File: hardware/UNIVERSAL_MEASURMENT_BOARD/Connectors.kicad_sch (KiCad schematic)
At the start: 43 parts, among them J1 2606-1110_010-000, J2 2606-1110_010-000, J28 FTSH-107-01-L-D-K, J3 2606-1110_010-000, J4 2606-1110_010-000, J5 2604-1104, U17 ESDS304DBVR, U18 ESDS304DBVR

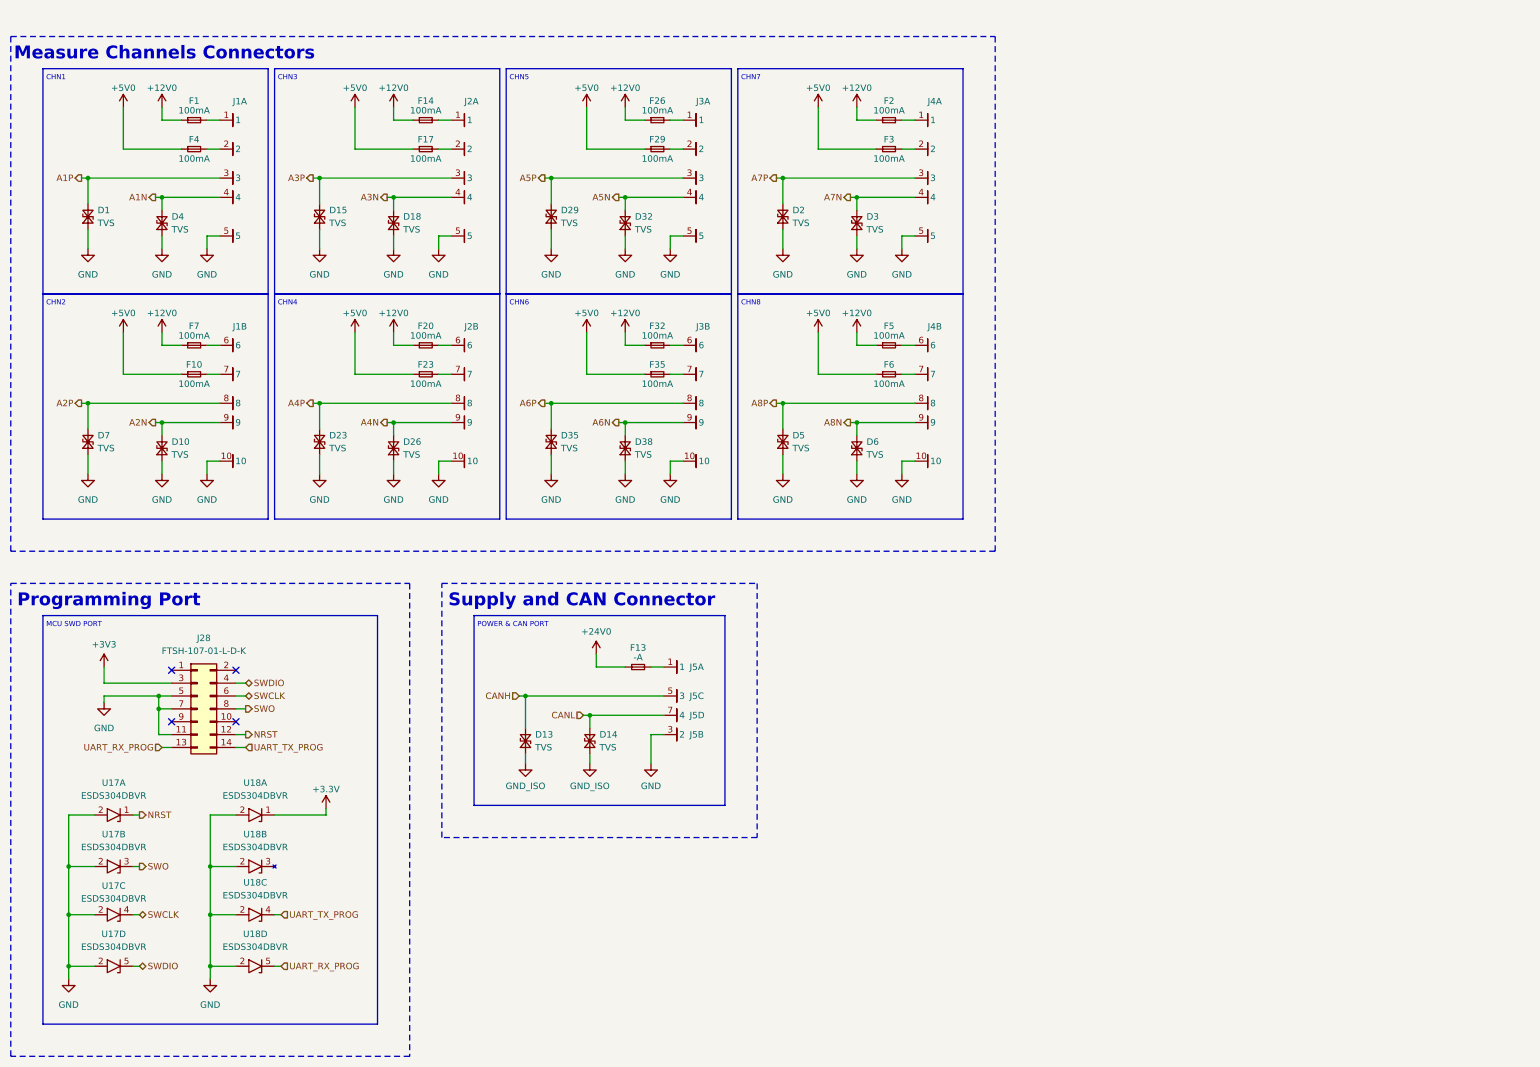
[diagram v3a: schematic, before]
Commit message: added footprints
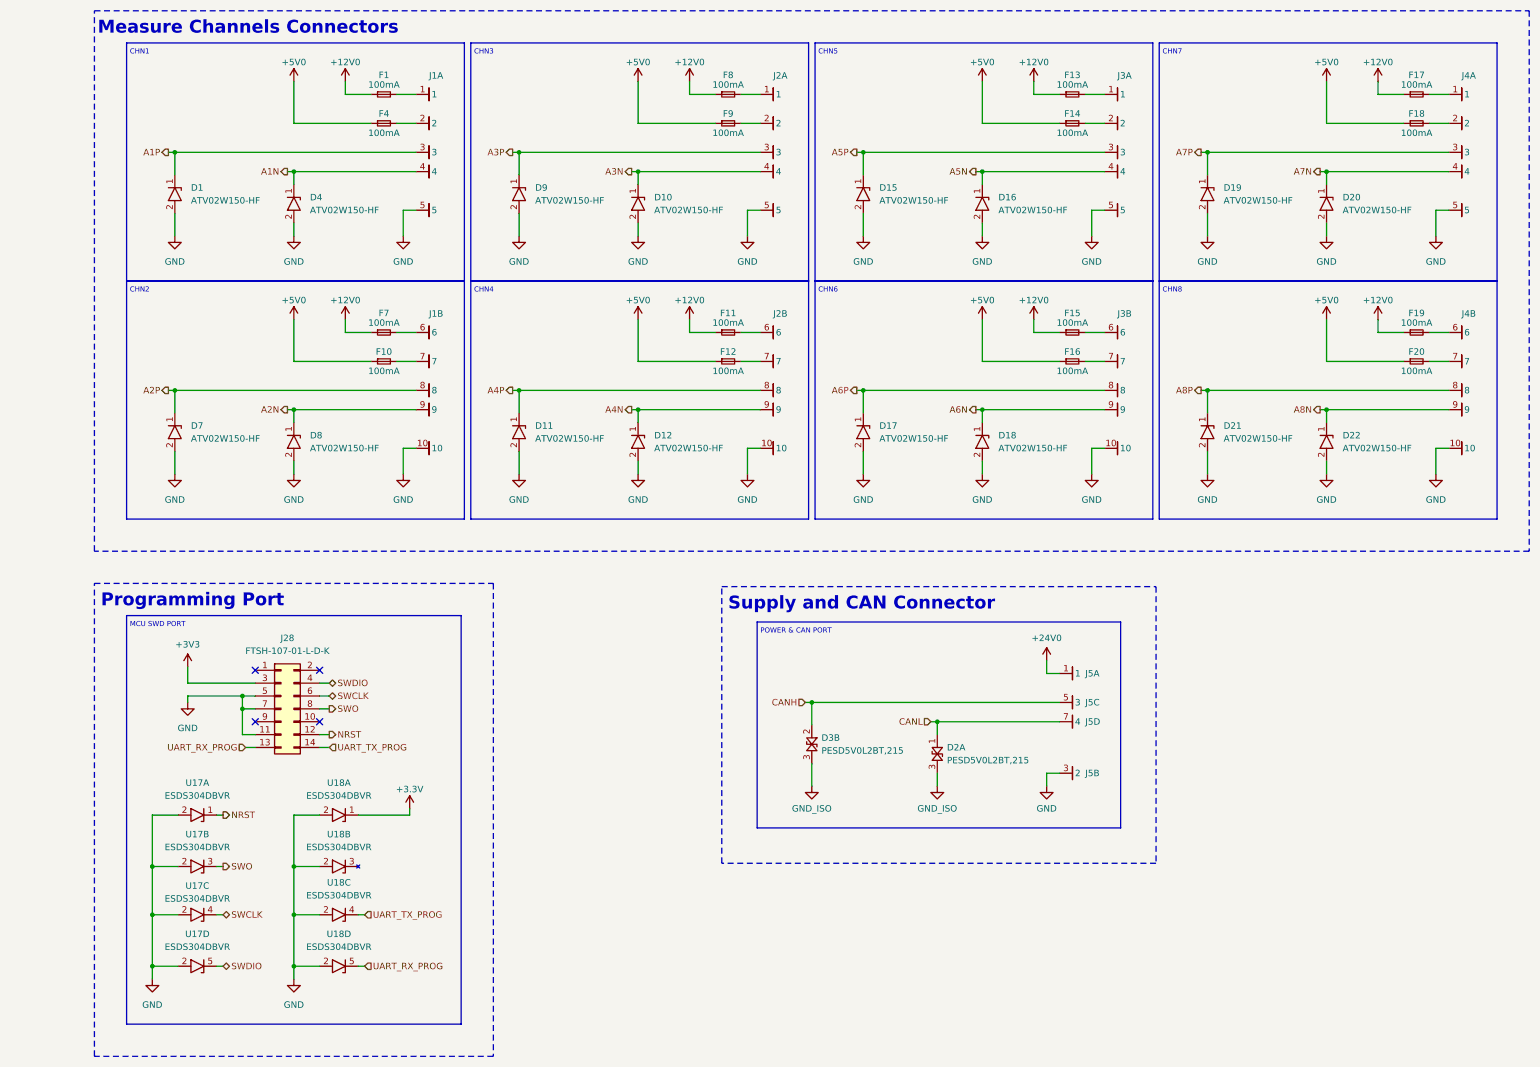
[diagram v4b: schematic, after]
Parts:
- removed D1, D10, D13, D14, D15, D18, D2, D23, D26, D29, D3, D32, D35, D38, D4, D5, D6, D7: TVS, symbol Device:D_TVS_Small
- removed F2, F23, F26, F29, F3, F32, F35, F5, F6: 100mA, symbol Device:Fuse_Small
- added D1, D10, D11, D12, D15, D16, D17, D18, D19, D20, D21, D22, D4, D7, D8, D9: ATV02W150-HF, SODFL3718X130N, symbol ATV02W150-HF:ATV02W150-HF
- added D2, D3: PESD5V0L2BT,215, SOT95P230X110-3N, symbol PESD5V0L2BT,215:PESD5V0L2BT,215
- added F11, F12, F15, F16, F18, F19, F8, F9: 100mA, Resistor_SMD:R_0603_1608Metric, symbol Device:Fuse_Small
- F1, F10, F14, F17, F20, F4, F7: footprint (none) -> Resistor_SMD:R_0603_1608Metric
- F13: value -A -> 100mA; footprint (none) -> Resistor_SMD:R_0603_1608Metric
- J28: footprint Samacsys:FTSH-107-XX-YYY-D-K -> FTSH-107-01-L-D-K:FTSH-107-XX-YYY-D-K
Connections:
- net +12V0: now also F13.1, F17.1, F11.1, F15.1, F19.1, F8.1; no longer F14.1, F20.1
- net +24V0: now also J5.1, J5.2 (1.2); no longer F13.1
- net +5V0: now also F14.1, F20.1, F12.1, F16.1, F18.1, F9.1; no longer F17.1
- net A1N: now also D4.1
- net A1P: now also D1.1
- net A2N: now also D8.1
- net A2P: now also D7.1
- net A3N: now also D10.1
- net A3P: now also D9.1
- net A4N: now also D12.1
- net A4P: now also D11.1
- net A5N: now also D16.1
- net A5P: now also D15.1
- net A6N: now also D18.1
- net A6P: now also D17.1
- net A7N: now also D20.1
- net A7P: now also D19.1
- net A8N: now also D22.1
- net A8P: now also D21.1
- net CANH: now also D3.2
- net CANL: now also D2.1
- net GND: now also D1.2, D10.2, D11.2, D12.2, D15.2, D16.2, D17.2, D18.2, D19.2, D20.2, D21.2, D22.2, D4.2, D7.2, D8.2, D9.2
- net GND_ISO: now also D2.3, D3.3
- net at J4.7: now also F20.2
- net at J3.7: now also F16.2
- net at J3.6: now also F15.2
- net at J4.6: now also F19.2
- net at J3.1: now also F13.2
- net at J2.7: now also F12.2
- net at J4.2: now also F18.2
- net at J2.6: now also F11.2; no longer F20.2
- net at J2.1: now also F8.2; no longer F14.2
- net at F17.2: now also J4.1; no longer J2.2
- net at J3.2: now also F14.2
- new net: F9.2, J2.2
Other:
- company: PUT Motorsport Formula Student team -> PUT Motorsport Formula Student Team
- moved on the sheet: F10, F7, J1A, J1B, J28, J2A, J2B, J3A, J3B, J4A, J4B, J5A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

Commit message: first outcom of pcb design
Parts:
- removed J5: 2604-1104, 2601-1104:26011104, symbol 2601-1104:2604-1104
- removed unit 2 of U17
- removed unit 4 of U18
- removed unit 3 of U18
- removed unit 1 of U18
- added J4, J5, J6, J7: Conn_01x01_Socket, REST:SolderWire-0.1sqmm_1x01_D0.4mm_OD1mm_Relief2x, symbol Connector:Conn_01x01_Socket
- added unit 4 of U16
- added unit 1 of U16
- added unit 2 of U16
- added unit 3 of U17
- F10: renamed from F11; footprint Resistor_SMD:R_0603_1608Metric -> REST:F_1206_3216Metric
- F11: renamed from F12; footprint Resistor_SMD:R_0603_1608Metric -> REST:F_1206_3216Metric
- F12: renamed from F13; footprint Resistor_SMD:R_0603_1608Metric -> REST:F_1206_3216Metric
- F13: renamed from F14; footprint Resistor_SMD:R_0603_1608Metric -> REST:F_1206_3216Metric
- F14: renamed from F15; footprint Resistor_SMD:R_0603_1608Metric -> REST:F_1206_3216Metric
- F15: renamed from F16; footprint Resistor_SMD:R_0603_1608Metric -> REST:F_1206_3216Metric
- F16: renamed from F17; footprint Resistor_SMD:R_0603_1608Metric -> REST:F_1206_3216Metric
- F17: renamed from F18; footprint Resistor_SMD:R_0603_1608Metric -> REST:F_1206_3216Metric
- F18: renamed from F19; footprint Resistor_SMD:R_0603_1608Metric -> REST:F_1206_3216Metric
- F19: renamed from F20; footprint Resistor_SMD:R_0603_1608Metric -> REST:F_1206_3216Metric
- F4: renamed from F1; footprint Resistor_SMD:R_0603_1608Metric -> REST:F_1206_3216Metric
- F5: renamed from F4; footprint Resistor_SMD:R_0603_1608Metric -> REST:F_1206_3216Metric
- F6: renamed from F7; footprint Resistor_SMD:R_0603_1608Metric -> REST:F_1206_3216Metric
- F7: renamed from F10; footprint Resistor_SMD:R_0603_1608Metric -> REST:F_1206_3216Metric
- F8, F9: footprint Resistor_SMD:R_0603_1608Metric -> REST:F_1206_3216Metric
- renumbered D12 to D10, D2 to D11, D3 to D11, D15 to D12, D17 to D13, D16 to D14, D18 to D15, D19 to D16, D21 to D17, D20 to D18, D22 to D19, D1 to D3, D7 to D4, D4 to D5, D8 to D6, D9 to D7, D11 to D8, D10 to D9, J28 to J1, J1 to J2, J2 to J3, J3 to J8, J4 to J9, U17 to U16, U18 to U17
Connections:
- net +24V0: now also J4.1 (Pin_1)
- net CANH: now also D11.1, J5.1 (Pin_1); no longer D11.2
- net CANL: now also D11.2, J6.1 (Pin_1); no longer D11.1
- net GND: now also J7.1 (Pin_1), U16.2, U16.2, U17.2
- net NRST: now also U17.4; no longer U17.1
- net SWDIO: now also U16.3; no longer U17.5
- net SWO: now also U16.5
- net UART_RX_PROG: now also U17.1
- net UART_TX_PROG: now also U17.5
- net +12V0 renamed +12V0A
- net +5V0 renamed +5V0A
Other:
- moved on the sheet: D11A, D11B

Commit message: Review fixes
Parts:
- J4, J5, J6, J7: footprint REST:SolderWire-0.1sqmm_1x01_D0.4mm_OD1mm_Relief2x -> REST:SolderPoint
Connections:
- net +3V3: now also U16.5
- net GND: now also U16.2, U17.4
- net NRST: now also U16.1; no longer U17.4
- net SWCLK: now also U17.1; no longer U16.4
- net SWDIO: now also U17.3; no longer U16.3
- net SWO: now also U17.5; no longer U16.5
- net UART_RX_PROG: now also U16.4; no longer U17.1
- net UART_TX_PROG: now also U16.3; no longer U17.5
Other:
- moved on the sheet: U16A

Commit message: clean up project visuals
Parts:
- J4, J5, J6, J7: value Conn_01x01_Socket -> Strain Relief
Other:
- moved on the sheet: D11A, D11B, J4, J5, J6, J7
